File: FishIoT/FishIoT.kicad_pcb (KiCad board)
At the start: 4 copper layers, 71.4 x 56.4 mm, 133 parts, among them IC1 RV-3032-C7_32.768KHZ-2.5PPM-T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, J1 VDD_JUMPER, J10 RM_UART, J11 Current Measurement, J13 UART_DEBUG, J2 0705430001, J3 SF72S006VBDR2500, J4 SHF-105-01-L-D-SM, J5 10119313-302TLF, J6 BM05B-ZESS-TBT, J8 BM05B-ZESS-TBT, J9 Conn_Coaxial, SW1 PTS645SM43SMTR92 LF, SW2 PTS645SM43SMTR92 LF, SW3 PTS645SM43SMTR92 LF, U1 NRF9160-SICA, U10 RM126x, U2 SKY65943-11, U3 TPD3F303DPVR, U4 TPS63000, U5 USBLC6-2P6, U6 CP2102N-Axx-xQFN20, U9 MAX3471

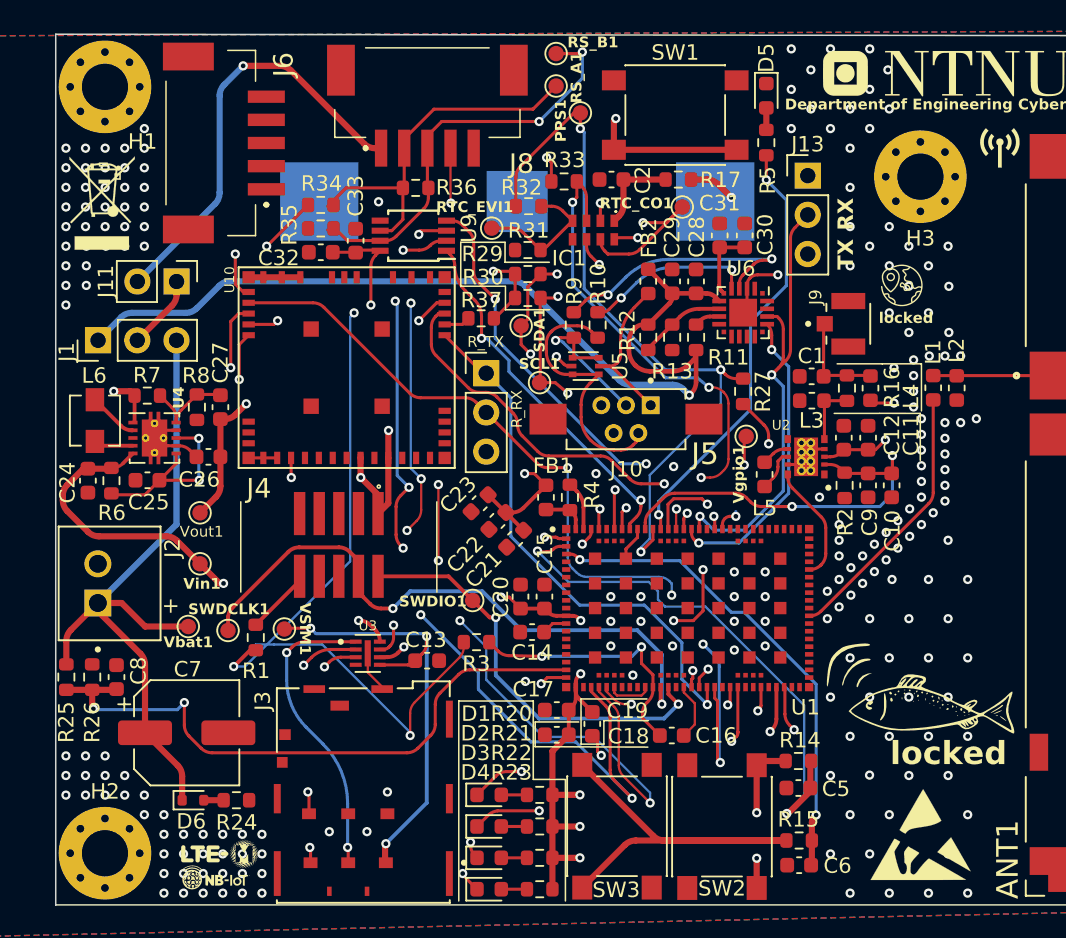
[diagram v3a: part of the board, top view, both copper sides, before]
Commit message: Fixed a bug on batteryvoltage for ADC input pin
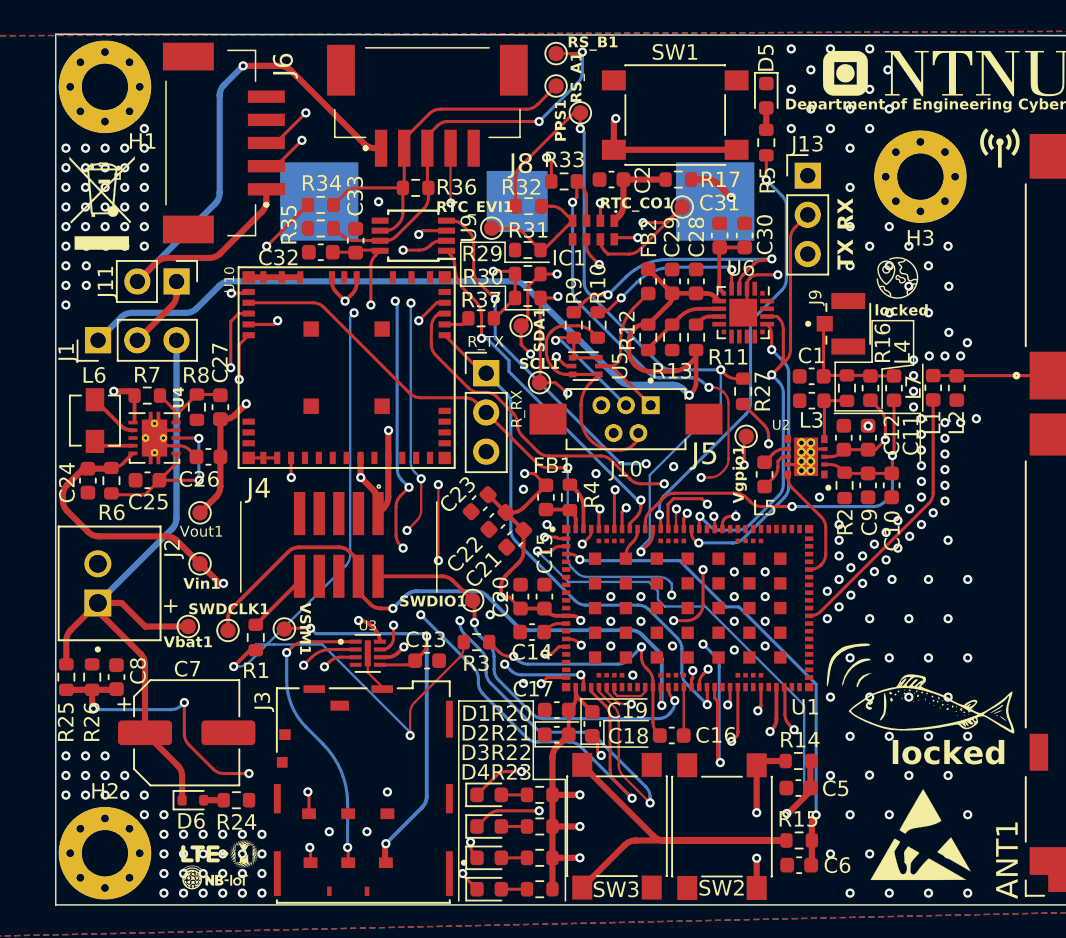
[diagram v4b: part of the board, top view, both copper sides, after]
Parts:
- added L7: 33nH, Inductor_SMD:L_0603_1608Metric, F.Cu at (221.7, 79.0)
- moved G*** 0.56 mm to (222.0, 71.9)
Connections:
- J6 pad 1: unconnected-(J6-Pin_1-Pad1) -> /VREG_IN
- J6 pad 2: unconnected-(J6-Pin_2-Pad2) -> /UART1_TX
- J6 pad 3: unconnected-(J6-Pin_3-Pad3) -> /UART1_RX
- J6 pad 4: unconnected-(J6-Pin_4-Pad4) -> GND
- U1 pad 15: unconnected-(U1-P0.08-Pad15) -> /UART1_TX
- U1 pad 16: unconnected-(U1-P0.09-Pad16) -> /UART1_RX
- U1 pad 19: /Battery_voltage -> unconnected-(U1-P0.11-Pad19)
- U1 pad 23: unconnected-(U1-P0.13/AIN0-Pad23) -> /Battery_voltage
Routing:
- net /UART1_RX: track 0.00 -> 48.0 mm, vias 0 -> 2
- net /UART1_TX: track 0.00 -> 46.4 mm, vias 0 -> 3
- net /VREG_IN: track 72.6 -> 84.0 mm
- net +3V3: track 89.1 -> 94.1 mm, vias 21 -> 19
- net /RM_CTS: track 52.8 -> 48.0 mm
- net /GPS_EN: track 26.2 -> 29.8 mm
- net GND: track 42.4 -> 45.4 mm, vias 212 -> 215
- net /Battery_voltage: track 41.3 -> 44.0 mm, vias 2 -> 5
- net Net-(J9-In): track 6.51 -> 8.04 mm
- net /RS485_A: track 23.7 -> 23.0 mm
- net /SWDIO: track 27.2 -> 26.5 mm
- net /RS485_B: track 27.2 -> 26.6 mm
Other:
- board text added: "A(+)"
- board text added: "B(-)"
- board text added: "GND"
- board text added: "JLCJLCJLCJLC"
- board text added: "PPS"
- board text added: "Vin"
